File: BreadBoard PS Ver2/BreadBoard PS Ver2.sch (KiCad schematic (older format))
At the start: 15 parts, among them J1 Barrel_Jack_Switch_MountingPin, J2 Conn_02x02_Odd_Even, J3 Conn_02x02_Odd_Even, J4 Conn_02x02_Odd_Even, J5 Conn_02x02_Odd_Even, SW1 SW_DPDT_x2, U1 LM7805_TO220

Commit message: Completed Schematic
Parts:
- R1: footprint (none) -> Resistor_THT:R_Axial_DIN0207_L6.3mm_D2.5mm_P7.62mm_Horizontal
- SW1: footprint (none) -> Button_Switch_THT:SW_CuK_JS202011CQN_DPDT_Straight
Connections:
- wire segments 28 -> 75
- no-connect marks 0 -> 3
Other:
- moved on the sheet: C1, C2, D1, D2, D3, D4, D5, J1, J2, J3, J4, J5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

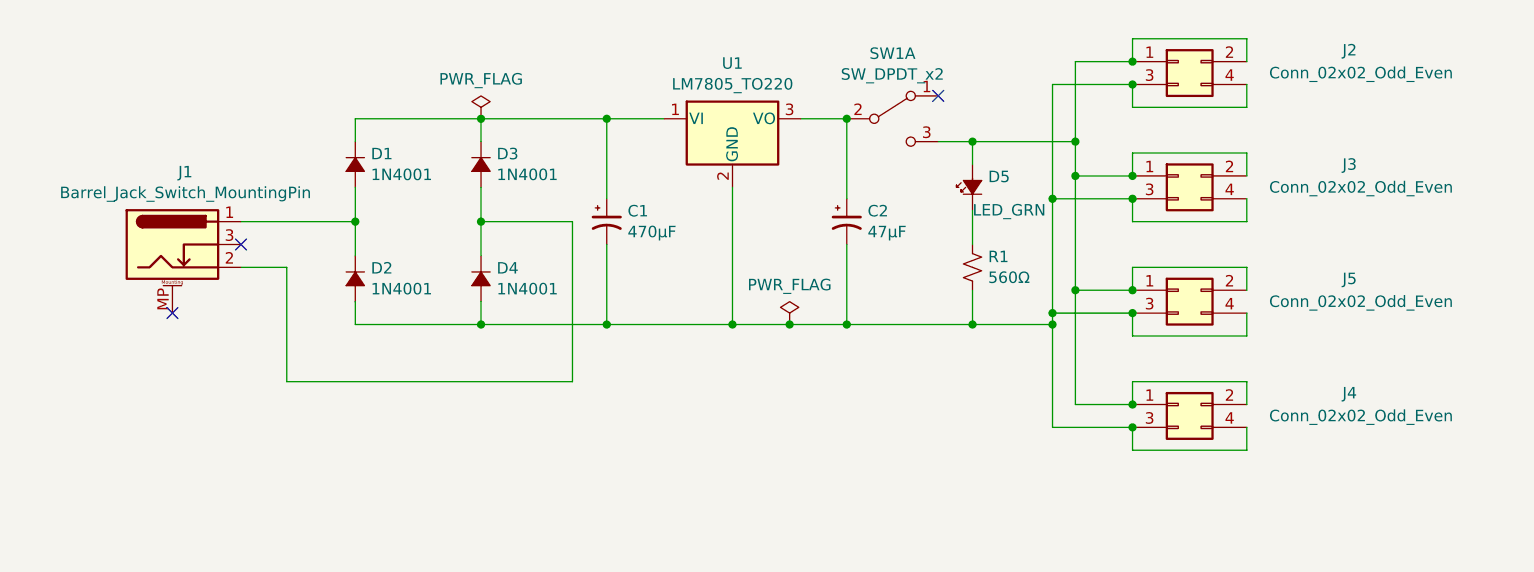
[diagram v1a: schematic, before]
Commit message: added Nets & ran Electrical Rules Check
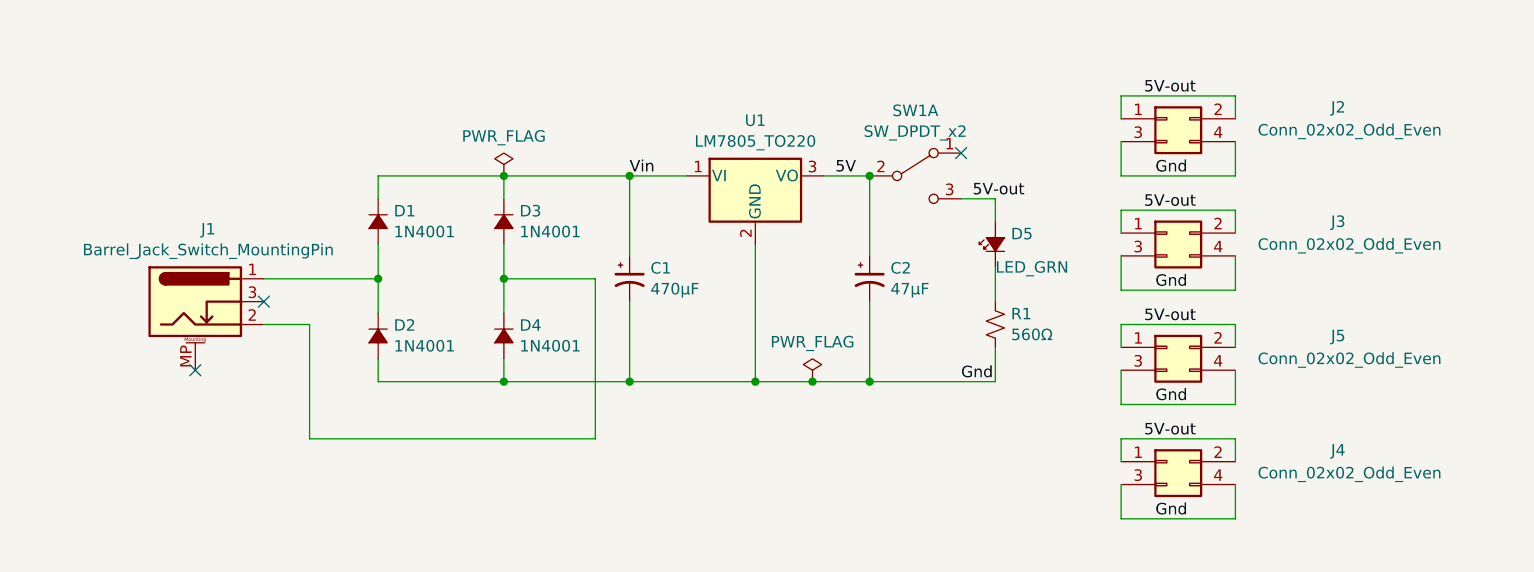
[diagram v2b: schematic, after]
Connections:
- net 5V: now reaches C2.1, SW1.2 (B), U1.3 (VO)
- net Gnd: now reaches C1.2, C2.2, D2.2 (A), D4.2 (A), J2.3 (Pin_3), J2.4 (Pin_4), J3.3 (Pin_3), J3.4 (Pin_4), J4.3 (Pin_3), J4.4 (Pin_4), J5.3 (Pin_3), J5.4 (Pin_4), R1.2, U1.2 (GND)
- net Vin: now reaches C1.1, D1.1 (K), D3.1 (K), U1.1 (VI)
- net 5V-out: now reaches D5.2 (A), J2.1 (Pin_1), J2.2 (Pin_2), J3.1 (Pin_1), J3.2 (Pin_2), J4.1 (Pin_1), J4.2 (Pin_2), J5.1 (Pin_1), J5.2 (Pin_2), SW1.3 (C)
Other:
- moved on the sheet: C1, C2, D1, D2, D3, D4, D5, J1, J2, J3, J4, J5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

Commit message: Added Net List
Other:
- note added: "5V Connectors"
- note added: "5V Regulator"
- note added: "DC Rectifier maintains +V"
- note added: "On/Off & Indicator"
- note added: "Power Input"
- moved on the sheet: J2, J3, J4, J5
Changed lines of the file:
@@
 L Connector_Generic:Conn_02x02_Odd_Even J2
 U 1 1 61B4BBCD
-P 7450 3050
-F 0 "J2" H 8200 3100 50  0000 C CNN
-F 1 "Conn_02x02_Odd_Even" H 8250 3000 50  0000 C CNN
-F 2 "Connector_PinHeader_2.54mm:PinHeader_2x02_P2.54mm_Vertical" H 7450 3050 50  0001 C CNN
-F 3 "~" H 7450 3050 50  0001 C CNN
-	1    7450 3050
+P 7350 3050
+F 0 "J2" H 8100 3100 50  0000 C CNN
+F 1 "Conn_02x02_Odd_Even" H 8150 3000 50  0000 C CNN
+F 2 "Connector_PinHeader_2.54mm:PinHeader_2x02_P2.54mm_Vertical" H 7350 3050 50  0001 C CNN
+F 3 "~" H 7350 3050 50  0001 C CNN
+	1    7350 3050
 	1    0    0    -1
 $EndComp
@@
 L Connector_Generic:Conn_02x02_Odd_Even J3
 U 1 1 61B4C628
-P 7450 3550
-F 0 "J3" H 8200 3600 50  0000 C CNN
-F 1 "Conn_02x02_Odd_Even" H 8250 3500 50  0000 C CNN
-F 2 "Connector_PinHeader_2.54mm:PinHeader_2x02_P2.54mm_Vertical" H 7450 3550 50  0001 C CNN
-F 3 "~" H 7450 3550 50  0001 C CNN
-	1    7450 3550
+P 7350 3550
+F 0 "J3" H 8100 3600 50  0000 C CNN
+F 1 "Conn_02x02_Odd_Even" H 8150 3500 50  0000 C CNN
+F 2 "Connector_PinHeader_2.54mm:PinHeader_2x02_P2.54mm_Vertical" H 7350 3550 50  0001 C CNN
+F 3 "~" H 7350 3550 50  0001 C CNN
+	1    7350 3550
 	1    0    0    -1
 $EndComp
@@
 L Connector_Generic:Conn_02x02_Odd_Even J5
 U 1 1 61B4D806
-P 7450 4050
-F 0 "J5" H 8200 4100 50  0000 C CNN
-F 1 "Conn_02x02_Odd_Even" H 8250 4000 50  0000 C CNN
-F 2 "Connector_PinHeader_2.54mm:PinHeader_2x02_P2.54mm_Vertical" H 7450 4050 50  0001 C CNN
-F 3 "~" H 7450 4050 50  0001 C CNN
-	1    7450 4050
+P 7350 4050
+F 0 "J5" H 8100 4100 50  0000 C CNN
+F 1 "Conn_02x02_Odd_Even" H 8150 4000 50  0000 C CNN
+F 2 "Connector_PinHeader_2.54mm:PinHeader_2x02_P2.54mm_Vertical" H 7350 4050 50  0001 C CNN
+F 3 "~" H 7350 4050 50  0001 C CNN
+	1    7350 4050
 	1    0    0    -1
 $EndComp
@@
 L Connector_Generic:Conn_02x02_Odd_Even J4
 U 1 1 61B4DDFA
-P 7450 4550
-F 0 "J4" H 8200 4600 50  0000 C CNN
-F 1 "Conn_02x02_Odd_Even" H 8250 4500 50  0000 C CNN
-F 2 "Connector_PinHeader_2.54mm:PinHeader_2x02_P2.54mm_Vertical" H 7450 4550 50  0001 C CNN
-F 3 "~" H 7450 4550 50  0001 C CNN
-	1    7450 4550
+P 7350 4550
+F 0 "J4" H 8100 4600 50  0000 C CNN
+F 1 "Conn_02x02_Odd_Even" H 8150 4500 50  0000 C CNN
+F 2 "Connector_PinHeader_2.54mm:PinHeader_2x02_P2.54mm_Vertical" H 7350 4550 50  0001 C CNN
+F 3 "~" H 7350 4550 50  0001 C CNN
+	1    7350 4550
 	1    0    0    -1
 $EndComp
@@
 NoConn ~ 6550 3200
 Wire Wire Line
-	7250 2950 7750 2950
-Wire Wire Line
-	7750 2950 7750 3050
-Wire Wire Line
-	7750 3550 7750 3450
-Wire Wire Line
-	7750 3450 7250 3450
-Wire Wire Line
-	7250 3450 7250 3550
-Wire Wire Line
-	7750 4050 7750 3950
-Wire Wire Line
-	7750 3950 7250 3950
-Wire Wire Line
-	7250 3950 7250 4050
-Wire Wire Line
-	7750 4550 7750 4450
-Wire Wire Line
-	7750 4450 7250 4450
-Wire Wire Line
-	7250 4450 7250 4550
+	7150 2950 7650 2950
+Wire Wire Line
+	7650 3450 7150 3450
+Wire Wire Line
+	7150 3450 7150 3550
+Wire Wire Line
+	7650 3950 7150 3950
+Wire Wire Line
+	7150 3950 7150 4050
+Wire Wire Line
+	7650 4450 7150 4450
+Wire Wire Line
+	7150 4450 7150 4550
 $Comp
 L power:PWR_FLAG #FLG0101
@@
 Wire Wire Line
 	6700 4050 6700 4200
-Text Label 7350 2950 0    50   ~ 0
-5V-out
-Wire Wire Line
-	7250 3050 7250 2950
-Text Label 7350 3450 0    50   ~ 0
-5V-out
-Text Label 7350 3950 0    50   ~ 0
-5V-out
-Text Label 7350 4450 0    50   ~ 0
-5V-out
-Wire Wire Line
-	7750 3300 7250 3300
-Wire Wire Line
-	7750 3150 7750 3300
-Wire Wire Line
-	7250 3150 7250 3300
-Wire Wire Line
-	7750 3800 7250 3800
-Wire Wire Line
-	7250 3650 7250 3800
-Wire Wire Line
-	7750 3650 7750 3800
-Wire Wire Line
-	7750 4300 7250 4300
-Wire Wire Line
-	7250 4150 7250 4300
-Wire Wire Line
-	7750 4150 7750 4300
-Wire Wire Line
-	7750 4800 7250 4800
-Wire Wire Line
-	7250 4650 7250 4800
-Wire Wire Line
-	7750 4650 7750 4800
-Text Label 7400 3300 0    50   ~ 0
-Gnd
-Text Label 7400 3800 0    50   ~ 0
-Gnd
-Text Label 7400 4300 0    50   ~ 0
-Gnd
-Text Label 7400 4800 0    50   ~ 0
-Gnd
+Text Label 7250 2950 0    50   ~ 0
+5V-out
+Wire Wire Line
+	7150 3050 7150 2950
+Text Label 7250 3450 0    50   ~ 0
+5V-out
+Text Label 7250 3950 0    50   ~ 0
+5V-out
+Text Label 7250 4450 0    50   ~ 0
+5V-out
+Wire Wire Line
+	7650 3300 7150 3300
+Wire Wire Line
+	7150 3150 7150 3300
+Wire Wire Line
+	7650 3800 7150 3800
+Wire Wire Line
+	7150 3650 7150 3800
+Wire Wire Line
+	7650 4300 7150 4300
+Wire Wire Line
+	7150 4150 7150 4300
+Wire Wire Line
+	7650 4800 7150 4800
+Wire Wire Line
+	7150 4650 7150 4800
+Text Label 7300 3300 0    50   ~ 0
+Gnd
+Text Label 7300 3800 0    50   ~ 0
+Gnd
+Text Label 7300 4300 0    50   ~ 0
+Gnd
+Text Label 7300 4800 0    50   ~ 0
+Gnd
+Wire Notes Line
+	3750 4900 3750 2750
+Wire Notes Line
+	3800 2750 3800 4900
+Wire Notes Line
+	3800 4900 4950 4900
+Wire Notes Line
+	4950 4900 4950 2750
+Wire Notes Line
+	4950 2750 3800 2750
+Wire Notes Line
+	5000 2750 5000 4900
+Wire Notes Line
+	5000 4900 6200 4900
+Wire Notes Line
+	6200 4900 6200 2750
+Wire Notes Line
+	6200 2750 5000 2750
+Wire Notes Line
+	6250 2750 6250 4900
+Wire Notes Line
+	7050 4900 7050 2750
+Wire Notes Line
+	6250 4900 7050 4900
+Wire Notes Line
+	6250 2750 7050 2750
+Wire Wire Line
+	7650 2950 7650 3050
+Wire Wire Line
+	7650 3150 7650 3300
+Wire Wire Line
+	7650 3450 7650 3550
+Wire Wire Line
+	7650 3650 7650 3800
+Wire Wire Line
+	7650 3950 7650 4050
+Wire Wire Line
+	7650 4150 7650 4300
+Wire Wire Line
+	7650 4450 7650 4550
+Wire Wire Line
+	7650 4650 7650 4800
+Wire Notes Line
+	7700 2750 7100 2750
+Wire Notes Line
+	7700 2750 7700 4900
+Wire Notes Line
+	7100 2750 7100 4900
+Wire Notes Line
+	7100 4900 7700 4900
+Wire Notes Line
+	2600 2750 2600 4900
+Wire Notes Line
+	3750 2750 2600 2750
+Wire Notes Line
+	3750 4900 2600 4900
+Text Notes 2950 2700 0    50   ~ 0
+Power Input
+Text Notes 3900 2700 0    50   ~ 0
+DC Rectifier maintains +V
+Text Notes 5250 2700 0    50   ~ 0
+5V Regulator
+Text Notes 6250 2700 0    50   ~ 0
+On/Off & Indicator
+Text Notes 7100 2700 0    50   ~ 0
+5V Connectors
 $EndSCHEMATC
